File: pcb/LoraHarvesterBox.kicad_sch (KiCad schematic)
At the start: 42 parts, among them J1 Conn_01x02_Pin, J2 Conn_01x02_Pin, J3 Conn_01x02_Pin, J4 Conn_01x04_Socket, J5 Conn_01x04_Socket, J6 Conn_01x04_Socket, J7 Conn_01x04_Socket, J8 Conn_01x06_Socket, SW1 SSSS811101, SW2 TS-1088-AR02016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

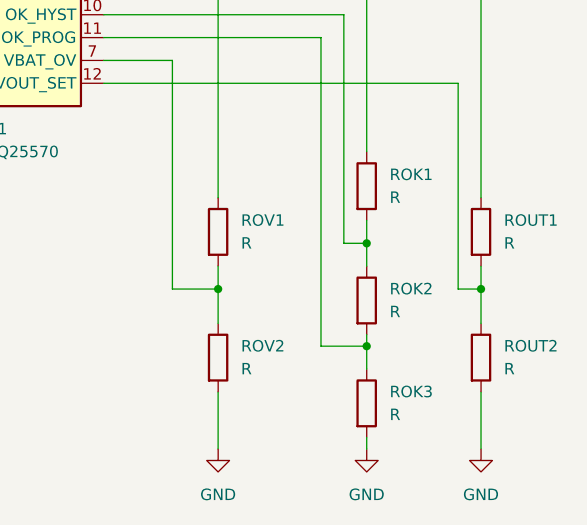
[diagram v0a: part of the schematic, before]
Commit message: docs, sch, pcb: yes.. now we lost schematic<->datasheet sync. fix annotation
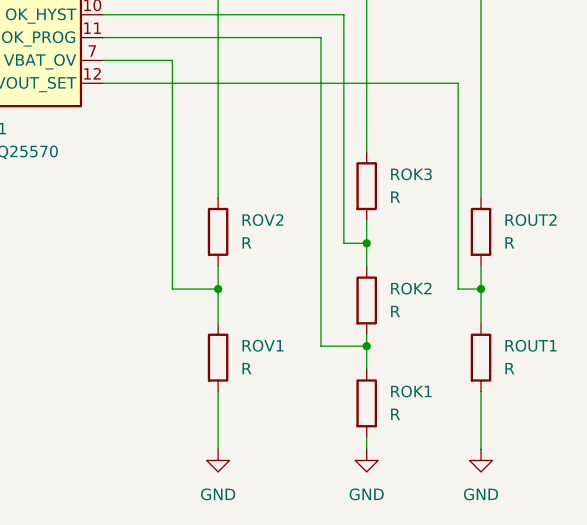
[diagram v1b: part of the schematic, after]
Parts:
- renumbered ROK3 to ROK1, ROK1 to ROK3, ROUT2 to ROUT1, ROUT1 to ROUT2, ROV2 to ROV1, ROV1 to ROV2
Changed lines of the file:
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@@
 		(dnp no)
 		(fields_autoplaced yes)
-		(property "Reference" "ROK1"
+		(property "Reference" "ROK3"
 			(at 375.92 203.1999 0)
 			(effects
@@
 			(project ""
 				(path "/a6f37965-abbf-44d1-94f3-9a9b9eaa16a8"
-					(reference "ROK1")
+					(reference "ROK3")
 					(unit 1)
 				)
@@
 		(dnp no)
 		(fields_autoplaced yes)
-		(property "Reference" "ROUT2"
+		(property "Reference" "ROUT1"
 			(at 388.62 222.2499 0)
 			(effects
@@
 			(project ""
 				(path "/a6f37965-abbf-44d1-94f3-9a9b9eaa16a8"
-					(reference "ROUT2")
+					(reference "ROUT1")
 					(unit 1)
 				)
@@
 		(dnp no)
 		(fields_autoplaced yes)
-		(property "Reference" "ROUT1"
+		(property "Reference" "ROUT2"
 			(at 388.62 208.2799 0)
 			(effects
@@
 			(project ""
 				(path "/a6f37965-abbf-44d1-94f3-9a9b9eaa16a8"
-					(reference "ROUT1")
+					(reference "ROUT2")
 					(unit 1)
 				)
@@
 		(dnp no)
 		(fields_autoplaced yes)
-		(property "Reference" "ROV1"
+		(property "Reference" "ROV2"
 			(at 359.41 208.2799 0)
 			(effects
@@
 			(project ""
 				(path "/a6f37965-abbf-44d1-94f3-9a9b9eaa16a8"
-					(reference "ROV1")
+					(reference "ROV2")
 					(unit 1)
 				)
@@
 		(dnp no)
 		(fields_autoplaced yes)
-		(property "Reference" "ROK3"
+		(property "Reference" "ROK1"
 			(at 375.92 227.3299 0)
 			(effects
@@
 			(project ""
 				(path "/a6f37965-abbf-44d1-94f3-9a9b9eaa16a8"
-					(reference "ROK3")
+					(reference "ROK1")
 					(unit 1)
 				)
@@
 		(dnp no)
 		(fields_autoplaced yes)
-		(property "Reference" "ROV2"
+		(property "Reference" "ROV1"
 			(at 359.41 222.2499 0)
 			(effects
@@
 			(project ""
 				(path "/a6f37965-abbf-44d1-94f3-9a9b9eaa16a8"
-					(reference "ROV2")
+					(reference "ROV1")
 					(unit 1)
 				)

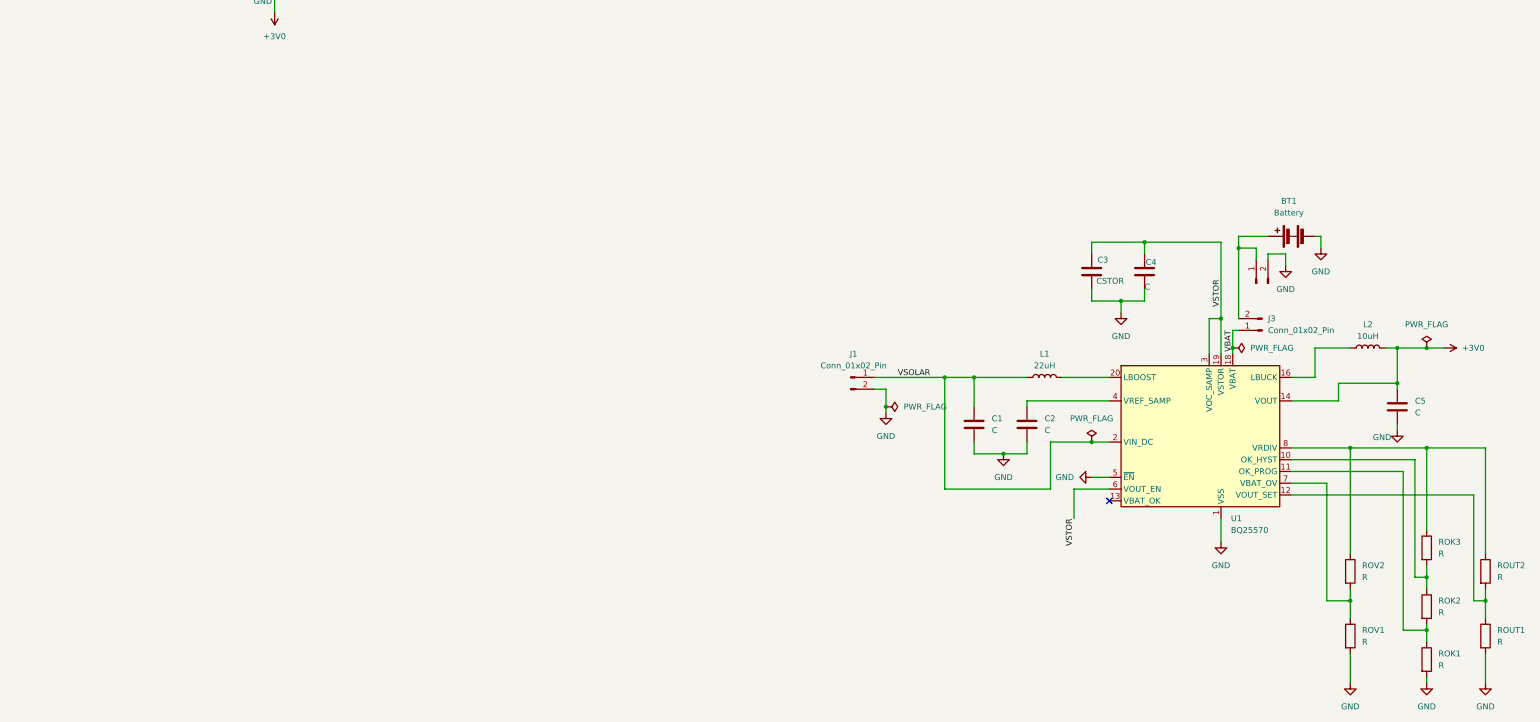
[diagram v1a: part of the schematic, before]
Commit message: pcb, sch: add resistor values and pretty up the pcb a bit
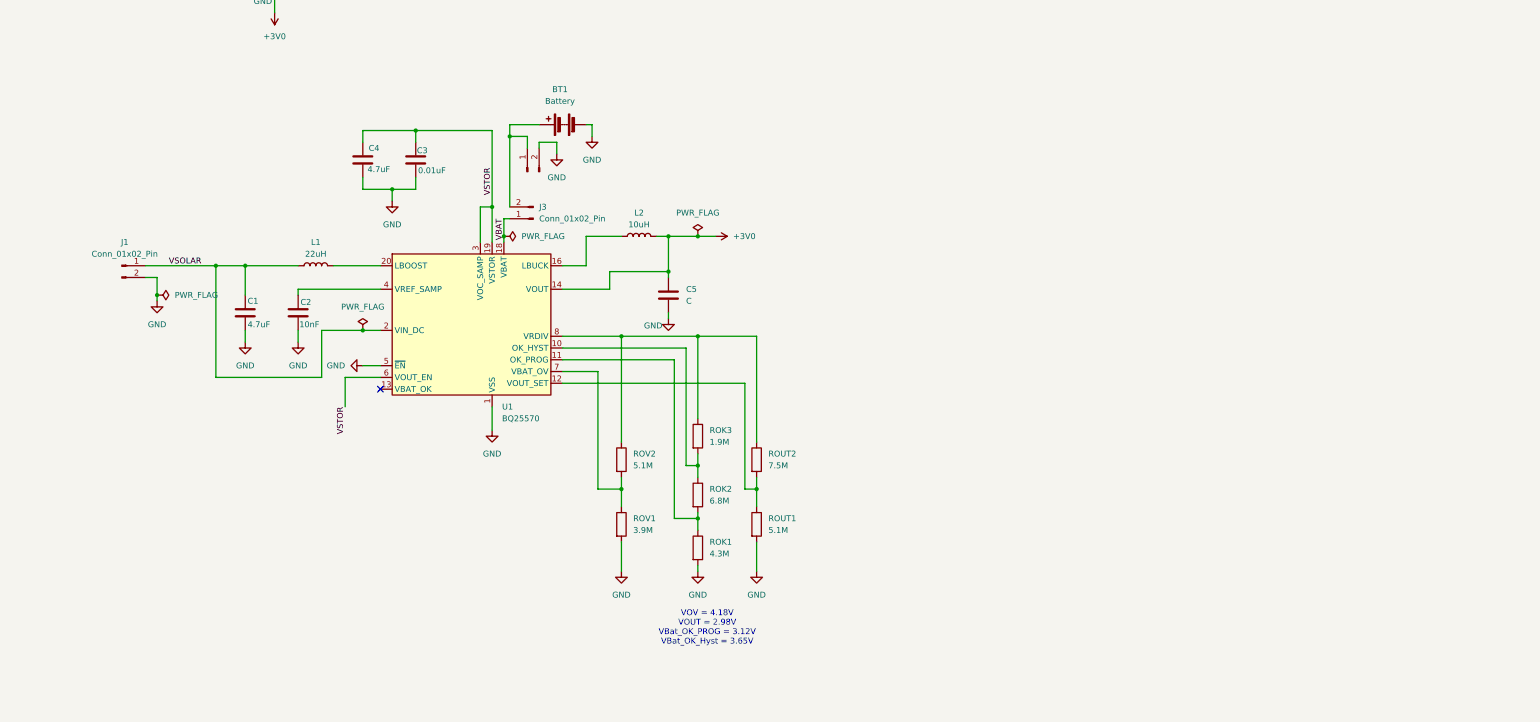
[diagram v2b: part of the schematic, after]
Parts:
- C1: value C -> 4.7uF
- C2: value C -> 10nF
- C3: renamed from C4; value C -> 0.01uF
- C4: renamed from C3; value CSTOR -> 4.7uF
- ROK1: value R -> 4.3M
- ROK2: value R -> 6.8M
- ROK3: value R -> 1.9M
- ROUT1, ROV2: value R -> 5.1M
- ROUT2: value R -> 7.5M
- ROV1: value R -> 3.9M
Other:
- note added: "VOV = 4.18V VOUT = 2.98V VBat_OK_PROG = 3.12V VBat_OK_Hyst = 3.65V"
- moved on the sheet: BT1, C1, C2, C3, C4, C5, J1, J3, L1, L2, ROK1, ROK2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

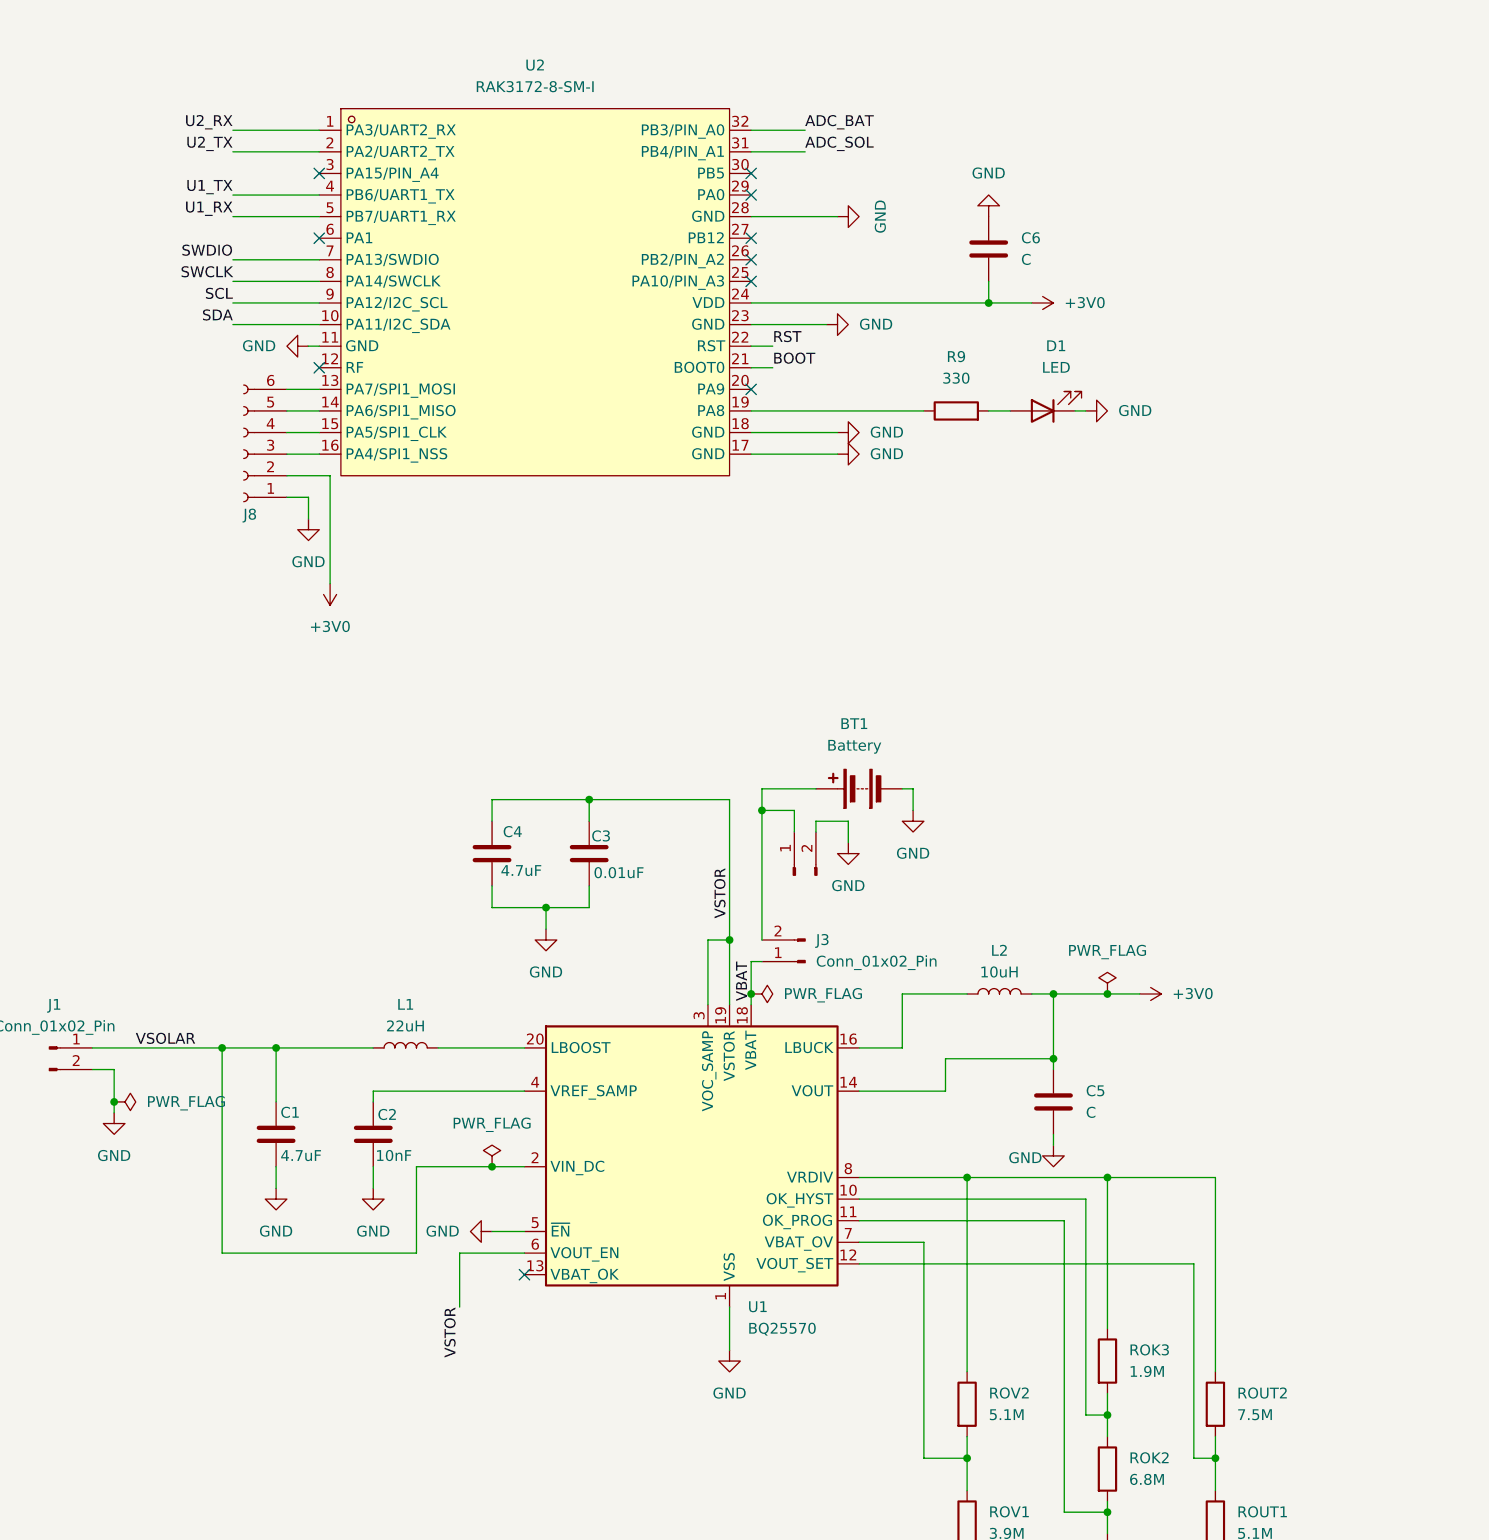
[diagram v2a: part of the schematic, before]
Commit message: pcb, sch: connect VBAT_OK signal to mirocontroller
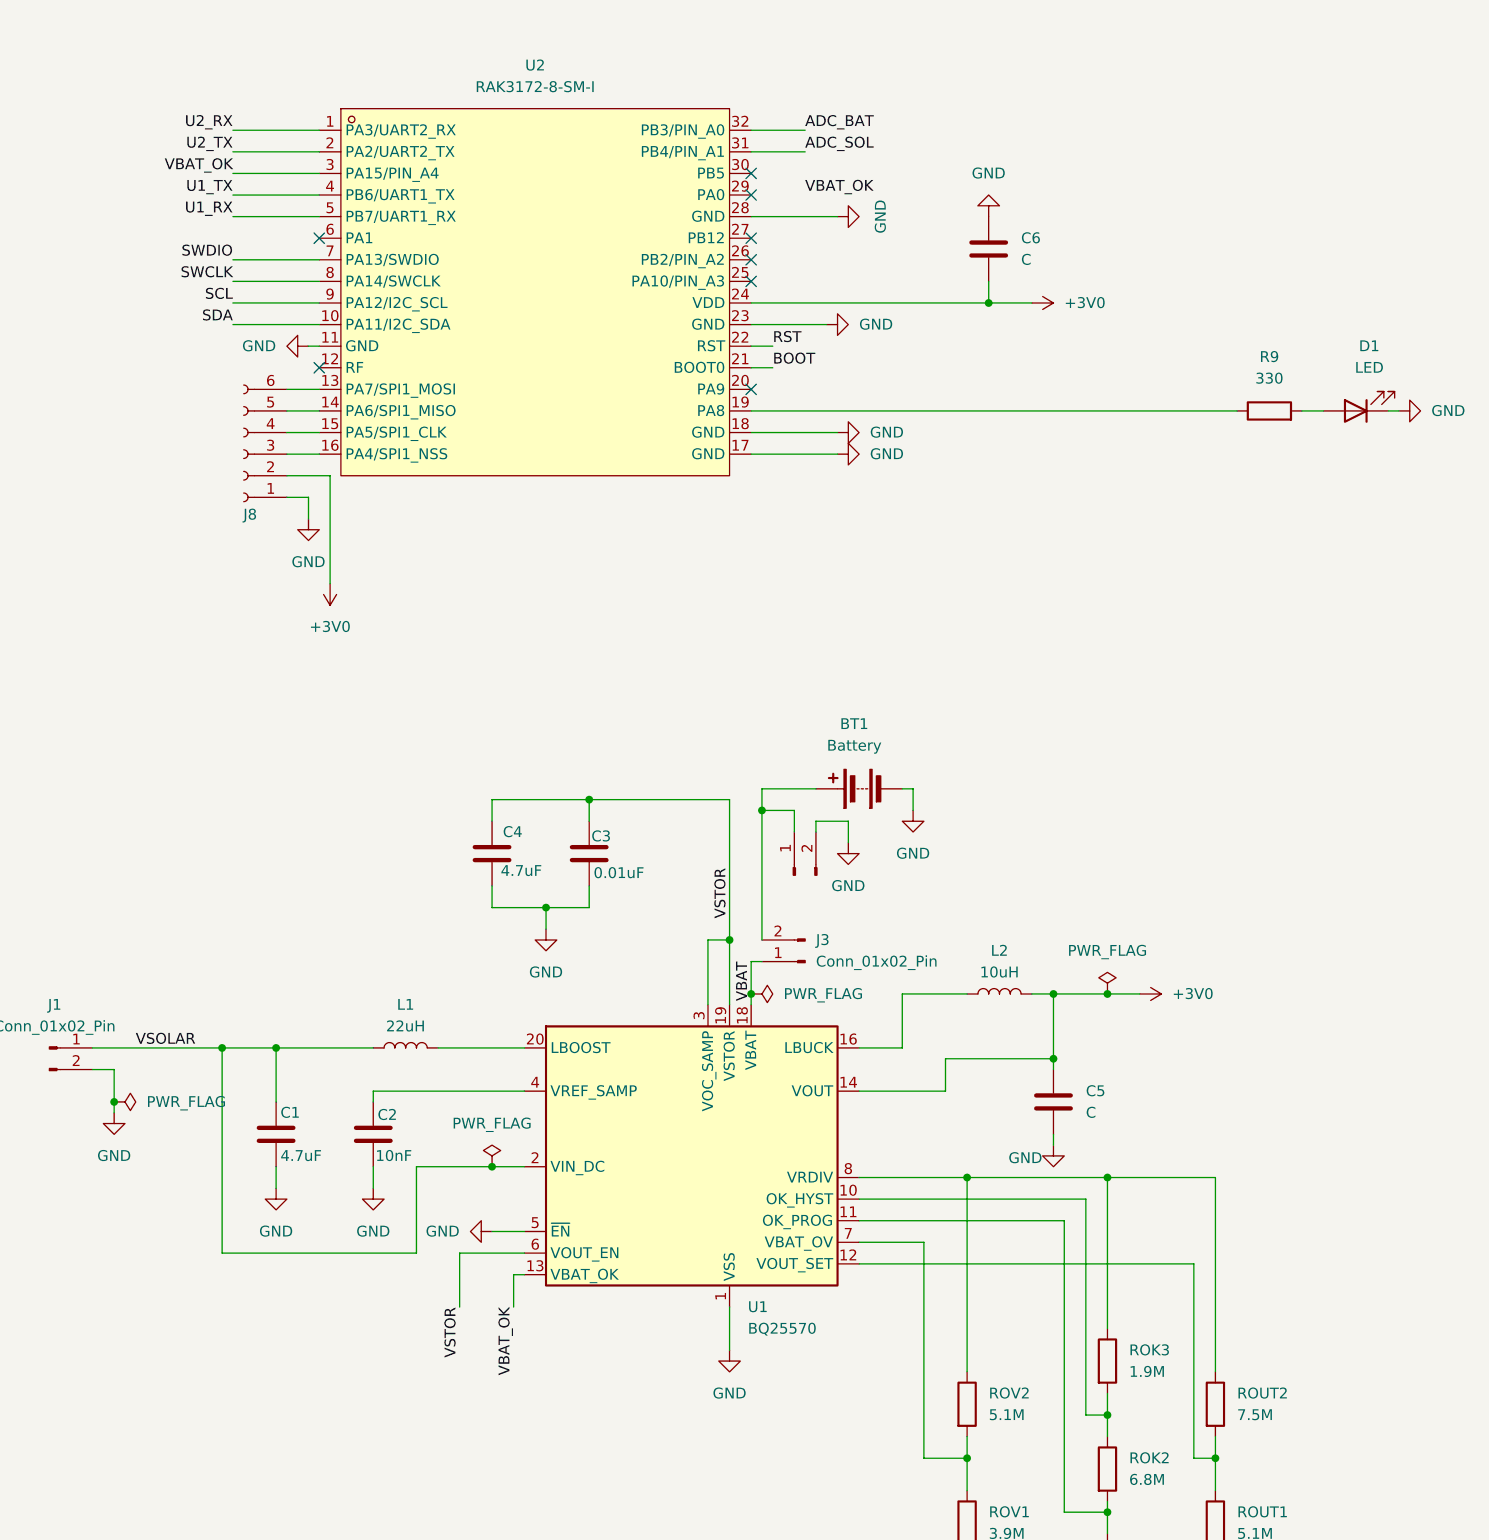
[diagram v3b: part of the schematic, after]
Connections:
- net VBAT_OK: now reaches U1.13 (VBAT_OK)
- net VBAT_OK: now also U2.3 (PA15/PIN_A4)
- no-connect marks 10 -> 8
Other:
- moved on the sheet: D1, R9
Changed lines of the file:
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@@
 	)
 	(no_connect
-		(at 147.32 170.18)
-	)
-	(no_connect
 		(at 173.99 50.8)
 	)
 	(no_connect
-		(at 123.19 40.64)
-	)
-	(no_connect
 		(at 173.99 43.18)
 	)
@@
 	(wire
 		(pts
+			(xy 146.05 170.18) (xy 146.05 173.99)
+		)
+		(stroke
+			(width 0)
+			(type default)
+		)
+	)
+	(wire
+		(pts
 			(xy 19.05 146.05) (xy 19.05 147.32)
 		)
@@
 	(wire
 		(pts
-			(xy 173.99 68.58) (xy 194.31 68.58)
+			(xy 173.99 68.58) (xy 231.14 68.58)
 		)
 		(stroke
@@
 	(wire
 		(pts
-			(xy 212.09 68.58) (xy 213.36 68.58)
+			(xy 248.92 68.58) (xy 250.19 68.58)
 		)
 		(stroke
@@
 	(wire
 		(pts
-			(xy 201.93 68.58) (xy 204.47 68.58)
+			(xy 238.76 68.58) (xy 241.3 68.58)
 		)
 		(stroke
@@
 	(wire
 		(pts
+			(xy 113.03 40.64) (xy 123.19 40.64)
+		)
+		(stroke
+			(width 0)
+			(type default)
+		)
+	)
+	(wire
+		(pts
 			(xy 168.91 138.43) (xy 168.91 130.81)
 		)
@@
 	(wire
 		(pts
+			(xy 147.32 170.18) (xy 146.05 170.18)
+		)
+		(stroke
+			(width 0)
+			(type default)
+		)
+	)
+	(wire
+		(pts
 			(xy 154.94 114.3) (xy 154.94 116.84)
 		)
@@
 		)
 	)
+	(label "VBAT_OK"
+		(at 146.05 173.99 270)
+		(effects
+			(font
+				(size 1.27 1.27)
+			)
+			(justify right bottom)
+		)
+	)
 	(label "SDA"
 		(at 113.03 58.42 180)
@@
 		)
 	)
+	(label "VBAT_OK"
+		(at 180.34 43.18 0)
+		(effects
+			(font
+				(size 1.27 1.27)
+			)
+			(justify left bottom)
+		)
+	)
 	(label "+3V0"
 		(at 46.99 25.4 270)
@@
 		)
 	)
+	(label "VBAT_OK"
+		(at 113.03 40.64 180)
+		(effects
+			(font
+				(size 1.27 1.27)
+			)
+			(justify right bottom)
+		)
+	)
 	(label "RST"
 		(at 176.53 60.96 0)
@@
 	(symbol
 		(lib_id "power:GND")
-		(at 213.36 68.58 90)
+		(at 250.19 68.58 90)
 		(unit 1)
 		(exclude_from_sim no)
@@
 		(fields_autoplaced yes)
 		(property "Reference" "#PWR035"
-			(at 219.71 68.58 0)
+			(at 256.54 68.58 0)
 			(effects
 				(font
@@
 		)
 		(property "Value" "GND"
-			(at 217.17 68.5799 90)
+			(at 254 68.5799 90)
 			(effects
 				(font
@@
 		)
 		(property "Footprint" ""
-			(at 213.36 68.58 0)
+			(at 250.19 68.58 0)
 			(effects
 				(font
@@
 		)
 		(property "Datasheet" ""
-			(at 213.36 68.58 0)
+			(at 250.19 68.58 0)
 			(effects
 				(font
@@
 		)
 		(property "Description" "Power symbol creates a global label with name \"GND\" , ground"
-			(at 213.36 68.58 0)
+			(at 250.19 68.58 0)
 			(effects
 				(font
@@
 	(symbol
 		(lib_id "Device:LED")
-		(at 208.28 68.58 180)
+		(at 245.11 68.58 180)
 		(unit 1)
 		(exclude_from_sim no)
@@
 		(fields_autoplaced yes)
 		(property "Reference" "D1"
-			(at 209.8675 60.96 0)
+			(at 246.6975 60.96 0)
 			(effects
 				(font
@@
 		)
 		(property "Value" "LED"
-			(at 209.8675 63.5 0)
+			(at 246.6975 63.5 0)
 			(effects
 				(font
@@
 		)
 		(property "Footprint" "LED_SMD:LED_0603_1608Metric"
-			(at 208.28 68.58 0)
+			(at 245.11 68.58 0)
 			(effects
 				(font
@@
 		)
 		(property "Datasheet" "~"
-			(at 208.28 68.58 0)
+			(at 245.11 68.58 0)
 			(effects
 				(font
@@
 		)
 		(property "Description" "Light emitting diode"
-			(at 208.28 68.58 0)
+			(at 245.11 68.58 0)
 			(effects
 				(font
@@
 		)
 		(property "Sim.Pins" "1=K 2=A"
-			(at 208.28 68.58 0)
+			(at 245.11 68.58 0)
 			(effects
 				(font
@@
 	(symbol
 		(lib_id "Device:R")
-		(at 198.12 68.58 90)
+		(at 234.95 68.58 90)
 		(unit 1)
 		(exclude_from_sim no)
@@
 		(fields_autoplaced yes)
 		(property "Reference" "R9"
-			(at 198.12 62.23 90)
+			(at 234.95 62.23 90)
 			(effects
 				(font
@@
 		)
 		(property "Value" "330"
-			(at 198.12 64.77 90)
+			(at 234.95 64.77 90)
 			(effects
 				(font
@@
 		)
 		(property "Footprint" "Resistor_SMD:R_01005_0402Metric_Pad0.57x0.30mm_HandSolder"
-			(at 198.12 70.358 90)
+			(at 234.95 70.358 90)
 			(effects
 				(font
@@
 		)
 		(property "Datasheet" "~"
-			(at 198.12 68.58 0)
+			(at 234.95 68.58 0)
 			(effects
 				(font
@@
 		)
 		(property "Description" "Resistor"
-			(at 198.12 68.58 0)
+			(at 234.95 68.58 0)
 			(effects
 				(font
